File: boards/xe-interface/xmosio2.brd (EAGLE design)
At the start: 116.8 x 55.2 mm, 105 parts, among them IC1 IDTQS3245QSOP20, IC2 IDTQS3245QSOP20, IC3 IDTQS3245QSOP20, IC4 IDTQS3245QSOP20, IC5 IDTQS3245QSOP20, U1 24 MHz Osc. (F535L-24), U2 USD-SOCKETNEW, X1 0446200002

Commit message: Fix the voltage supervisor circuit, so we can bring up the 1v rail
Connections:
- net VCCINT: no longer U$6.5
- net VCCIO: now also U$6.5
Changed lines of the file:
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@@
 <contactref element="R6" pad="2"/>
 <contactref element="C32" pad="+"/>
-<contactref element="U$6" pad="5"/>
 <contactref element="U$11" pad="5"/>
 <wire x1="64.4525" y1="25.82" x2="69.5325" y2="25.82" width="0" layer="19" extent="1-1"/>
@@
 <wire x1="46.57" y1="16.03375" x2="48.68" y2="21.43125" width="0" layer="19" extent="1-1"/>
 <wire x1="46.57" y1="13.335" x2="46.57" y2="16.03375" width="0" layer="19" extent="1-1"/>
-<wire x1="40.28375" y1="25.4" x2="48.895" y2="24.8675" width="0" layer="19" extent="1-1"/>
-<wire x1="37.62375" y1="25.99" x2="40.28375" y2="25.4" width="0" layer="19" extent="1-1"/>
+<wire x1="37.465" y1="12.185" x2="46.57" y2="13.335" width="0" layer="19" extent="1-1"/>
+<wire x1="37.62375" y1="25.99" x2="48.895" y2="24.8675" width="0" layer="19" extent="1-1"/>
 <wire x1="31.75" y1="24.905" x2="37.62375" y2="25.99" width="0" layer="19" extent="1-1"/>
-<wire x1="37.465" y1="12.185" x2="46.57" y2="13.335" width="0" layer="19" extent="1-1"/>
 <wire x1="41.43375" y1="37.9975" x2="37.62375" y2="25.99" width="0" layer="19" extent="1-1"/>
 </signal>
@@
 <contactref element="LED1" pad="A"/>
 <contactref element="R15" pad="2"/>
+<contactref element="U$6" pad="5"/>
 <wire x1="104.394" y1="18.8205" x2="107.442" y2="18.094" width="0" layer="19" extent="1-1"/>
 <wire x1="104.394" y1="14.3755" x2="104.394" y2="18.8205" width="0" layer="19" extent="1-1"/>
@@
 <wire x1="35.56" y1="17.995" x2="38.4175" y2="17.995" width="0" layer="19" extent="1-1"/>
 <wire x1="40.28375" y1="24.45" x2="38.4175" y2="17.995" width="0" layer="19" extent="1-1"/>
-<wire x1="45.085" y1="26.5675" x2="40.28375" y2="24.45" width="0" layer="19" extent="1-1"/>
+<wire x1="40.28375" y1="25.4" x2="40.28375" y2="24.45" width="0" layer="19" extent="1-1"/>
+<wire x1="45.085" y1="26.5675" x2="40.28375" y2="25.4" width="0" layer="19" extent="1-1"/>
 <wire x1="45.24375" y1="30.10625" x2="45.085" y2="26.5675" width="0" layer="19" extent="1-1"/>
 <wire x1="48.9585" y1="31.7745" x2="45.24375" y2="30.10625" width="0" layer="19" extent="1-1"/>

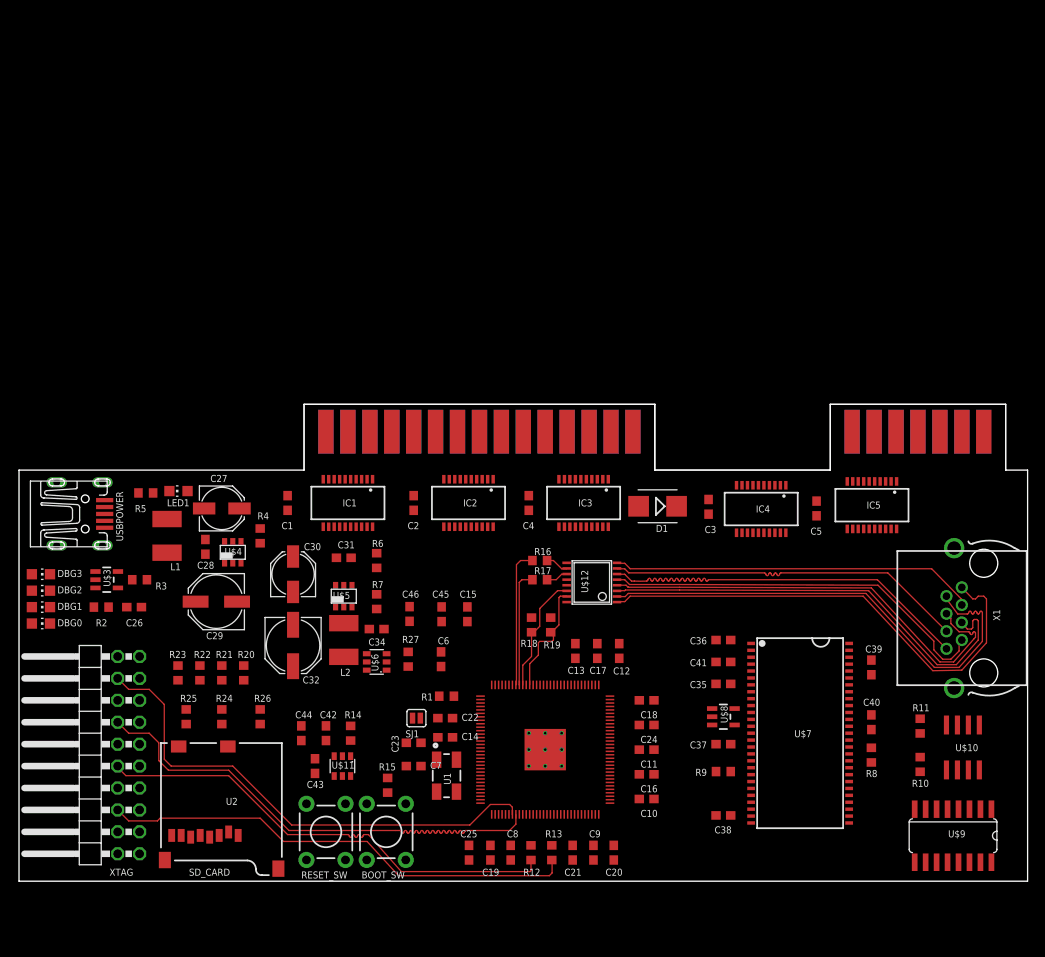
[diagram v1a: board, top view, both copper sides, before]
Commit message: Move to a SeeedStudio style layout (far cheaper, and we can get assembly as part of the package). We still require the 5/5 spacing though.
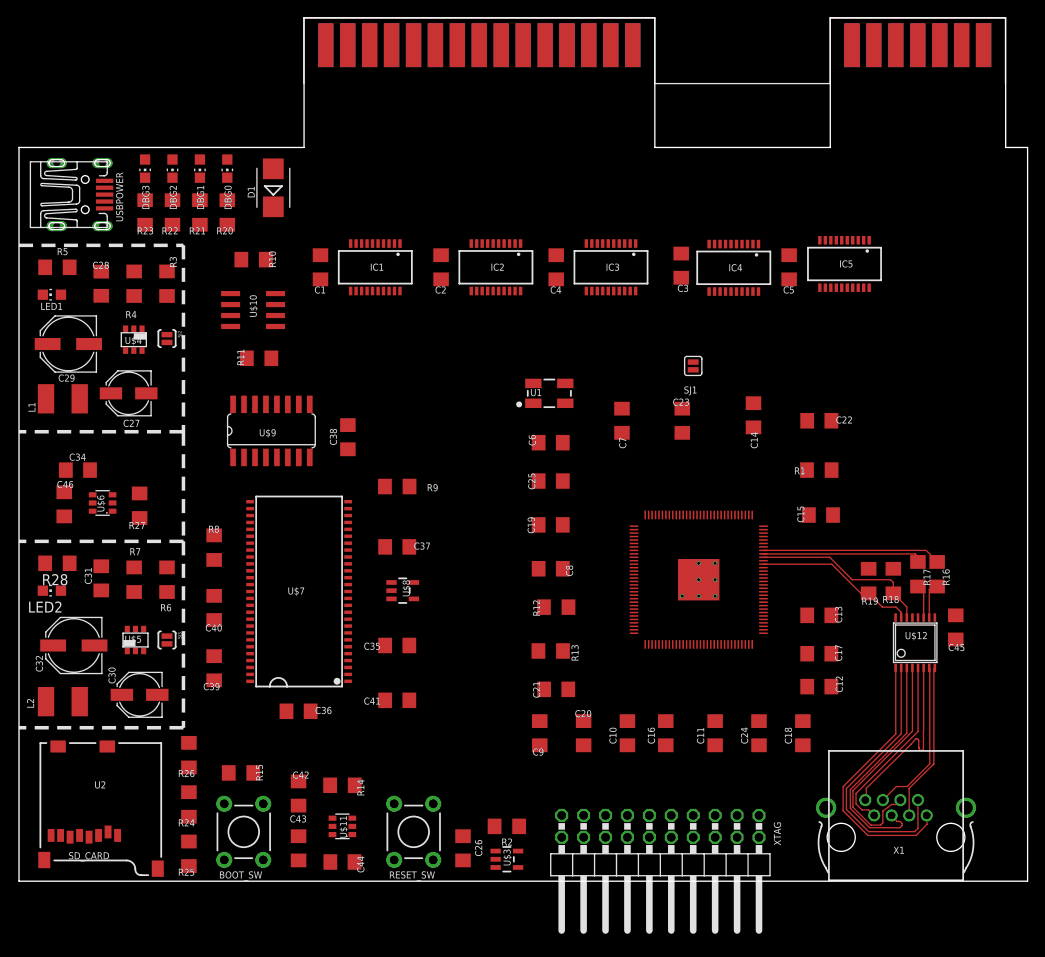
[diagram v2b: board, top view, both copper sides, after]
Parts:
- added LED2: ok33, led:CHIP-LED0805
- added R28: 47R, rcl:R1206
- added SJ2, SJ3: SOLDERJUMPERNO, SparkFun:SJ_2S-NO
- C1, C10, C11, C12, C13, C14, C15, C16, C17, C18, C19, C2, C20, C21, C22, C23, C24, C25, C26, C28, C3, C31, C34, C35, C36, C37, C38, C39, C4, C40, C41, C42, C43, C44, C45, C46, C5, C6, C7, C8, C9: device rcl:C0603 -> rcl:C1206
- R1, R10, R11, R12, R13, R14, R15, R16, R17, R18, R19, R2, R20, R21, R22, R23, R24, R25, R26, R27, R3, R4, R5, R6, R7, R8, R9: device rcl:R0603 -> rcl:R1206
- moved R10 96.9 mm to (27.2, 72.0), turned to 0 degrees
- moved U$10 96.6 mm to (27.1, 66.2), turned to 90 degrees
- moved U$9 91.8 mm to (29.2, 52.2), turned to 0 degrees
- moved R11 87.6 mm to (27.8, 60.6), turned to 0 degrees
- moved R8 79.8 mm to (22.6, 38.6), turned to 90 degrees
- moved C40 77.3 mm to (22.6, 31.7), turned to 90 degrees
- moved C39 76.1 mm to (22.6, 24.7), turned to 270 degrees
- moved XTAG 68.0 mm to (74.3, 1.27), turned to 180 degrees
- moved C38 61.7 mm to (38.1, 51.4), turned to 90 degrees
- moved U$7 60.3 mm to (32.4, 33.6), turned to 90 degrees
- moved C45 59.6 mm to (108.5, 29.4), turned to 90 degrees
- moved D1 57.8 mm to (29.5, 80.3), turned to 90 degrees
- moved DBG0 57.0 mm to (24.1, 82.5), turned to 180 degrees
- moved U$3 56.5 mm to (56.5, 2.54)
- moved C22 55.4 mm to (92.7, 53.3)
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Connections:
- new net N$30: C29.+, L1.1, LED1.A, R3.2, SJ2.1
- new net N$31: LED2.C, R28.2
- new net N$32: C32.+, L2.1, LED2.A, R6.2, SJ3.1
- net GND: now also R28.1
- net VCCINT: now also SJ3.2; no longer C32.+, L2.1, R6.2
- net VCCIO: now also SJ2.2; no longer C29.+, L1.1, LED1.A, R3.2
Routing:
- net JTAG_DN1: track 58.4 -> 0.00 mm
- net JTAG_DN0: track 57.1 -> 0.00 mm
- net JTAG_UP1: track 55.5 -> 0.00 mm
- net JTAG_UP0: track 55.3 -> 0.00 mm
- net RIN1_N: track 57.0 -> 31.6 mm
- net RIN1_P: track 57.0 -> 31.8 mm
- net RIN2_N: track 52.1 -> 27.4 mm
- net RIN2_P: track 52.4 -> 27.9 mm
- net DOUT2_N: track 45.8 -> 21.4 mm
- net DOUT1_N: track 42.4 -> 18.3 mm
- net DOUT2_P: track 44.8 -> 20.9 mm
- net DOUT1_P: track 42.0 -> 18.3 mm
- net LNK_IN0: track 13.8 -> 21.0 mm
- net LNK_IN1: track 13.6 -> 18.9 mm
- net N$28: track 13.5 -> 18.6 mm
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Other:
- board size 116.8 x 55.2 mm -> 116.8 x 100 mm

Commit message: Latest fixes and additions  - screw holes  - cartridge slot  - PBI device selection DIP switch  - Memory interface style DIP switch
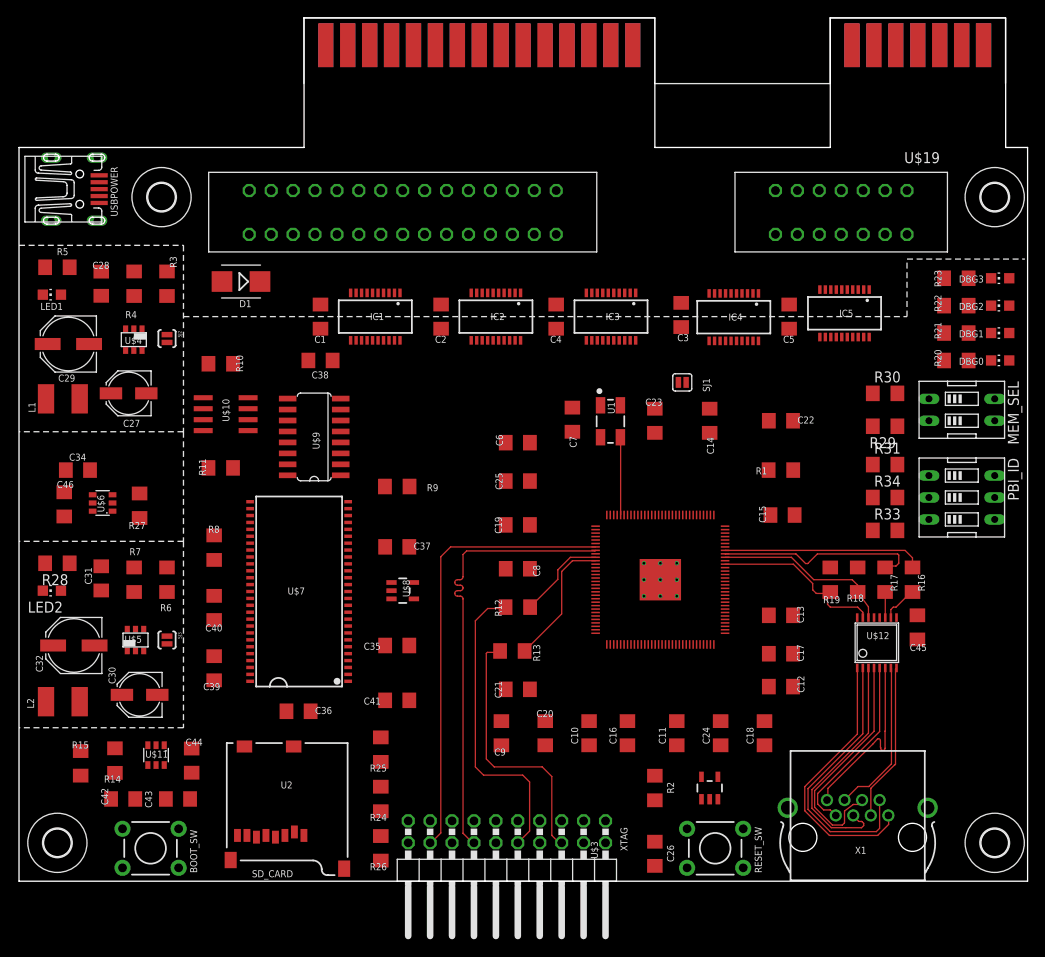
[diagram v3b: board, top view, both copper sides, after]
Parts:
- added H1, H2, H3, H4: MOUNT-HOLE3.2, holes:3,2
- added MEM_SEL: (no value), special:EDG-02
- added PBI_ID: (no value), special:EDG-03
- added R29, R30, R31, R33, R34: 10K, rcl:R1206
- added U$19: XE_SLOT, pbxl:XE_SLOT
- moved DBG3 99.9 mm to (113.7, 69.8), turned to 90 degrees
- moved DBG2 97.2 mm to (113.7, 66.7), turned to 90 degrees
- moved DBG1 94.6 mm to (113.7, 63.5), turned to 90 degrees
- moved R23 94.3 mm to (108.6, 69.8), turned to 180 degrees
- moved DBG0 92.3 mm to (113.7, 60.3), turned to 90 degrees
- moved R22 91.4 mm to (108.6, 66.7), turned to 180 degrees
- moved R21 88.7 mm to (108.6, 63.5), turned to 180 degrees
- moved R20 86.2 mm to (108.6, 60.3), turned to 180 degrees
- moved RESET_SW 35.0 mm to (80.6, 3.81), turned to 0 degrees
- moved R14 26.5 mm to (11.1, 14.0), turned to 270 degrees
- moved R25 25.3 mm to (41.9, 15.2)
- moved U$3 24.9 mm to (80.0, 10.8), turned to 0 degrees
- moved R26 24.7 mm to (41.9, 3.81)
- moved U$11 23.1 mm to (15.9, 14.6), turned to 180 degrees
- moved R24 22.2 mm to (41.9, 9.53)
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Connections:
- new net N$34: MEM_SEL.2, R29.1, U$2.25
- new net N$35: MEM_SEL.1, R30.2, U$2.26
- new net PBI0: PBI_ID.1, R31.2, U$2.33
- new net PBI1: PBI_ID.2, R34.2, U$2.61
- new net PBI2: PBI_ID.3, R33.2, U$2.62
- net +5V: now also U$19.26, U$19.44
- net B1: now also U$19.1
- net B10: now also U$19.11
- net B11: now also U$19.12
- net B12: now also U$19.13
- net B13: now also U$19.14
- net B14: now also U$19.15
- net B15: now also U$19.16
- net B16: now also U$19.17
- net B17: now also U$19.18
- net B18: now also U$19.19
- net B19: now also U$19.20
- net B2: now also U$19.2
- net B20: now also U$19.21
- net B21: now also U$19.22
- net B22: now also U$19.23
- net B23: now also U$19.24
- net B24: now also U$19.25
- net B25: now also U$19.27
- net B26: now also U$19.28
- net B27: now also U$19.29
- net B28: now also U$19.30
- net B29: now also U$19.32
- net B3: now also U$19.4
- net B30: now also U$19.33
- net B31: now also U$19.34
- net B32: now also U$19.35
- net B33: now also U$19.36
- net B34: now also U$19.37
- net B35: now also U$19.38
- net B36: now also U$19.39
- net B37: now also U$19.41
- net B38: now also U$19.42
- net B4: now also U$19.5
- net B5: now also U$19.6
- net B6: now also U$19.7
- net B7: now also U$19.8
- net B8: now also U$19.9
- net B9: now also U$19.10
- net GND: now also R29.2, R30.1, R31.1, R33.1, R34.1, U$19.3, U$19.43
- net VCCIO: now also MEM_SEL.3, MEM_SEL.4, PBI_ID.4, PBI_ID.5, PBI_ID.6
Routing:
- net JTAG_DN1: track 0.00 -> 52.1 mm
- net JTAG_DN0: track 0.00 -> 51.9 mm
- net JTAG_UP0: track 0.00 -> 35.7 mm
- net JTAG_UP1: track 0.00 -> 30.7 mm
- net N$23: track 0.00 -> 15.4 mm
- net N$22: track 0.00 -> 10.6 mm
- net N$2: track 0.00 -> 9.01 mm
- net N$28: track 18.6 -> 23.8 mm
- net N$29: track 20.7 -> 23.2 mm
- net LNK_IN1: track 18.9 -> 20.8 mm
- net LNK_OUT0: track 4.18 -> 3.52 mm
